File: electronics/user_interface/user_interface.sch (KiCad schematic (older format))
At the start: 48 parts, among them J1 Conn_01x06, J2 Conn_02x05_Odd_Even, U1 PCF8574, U2 PCF8574

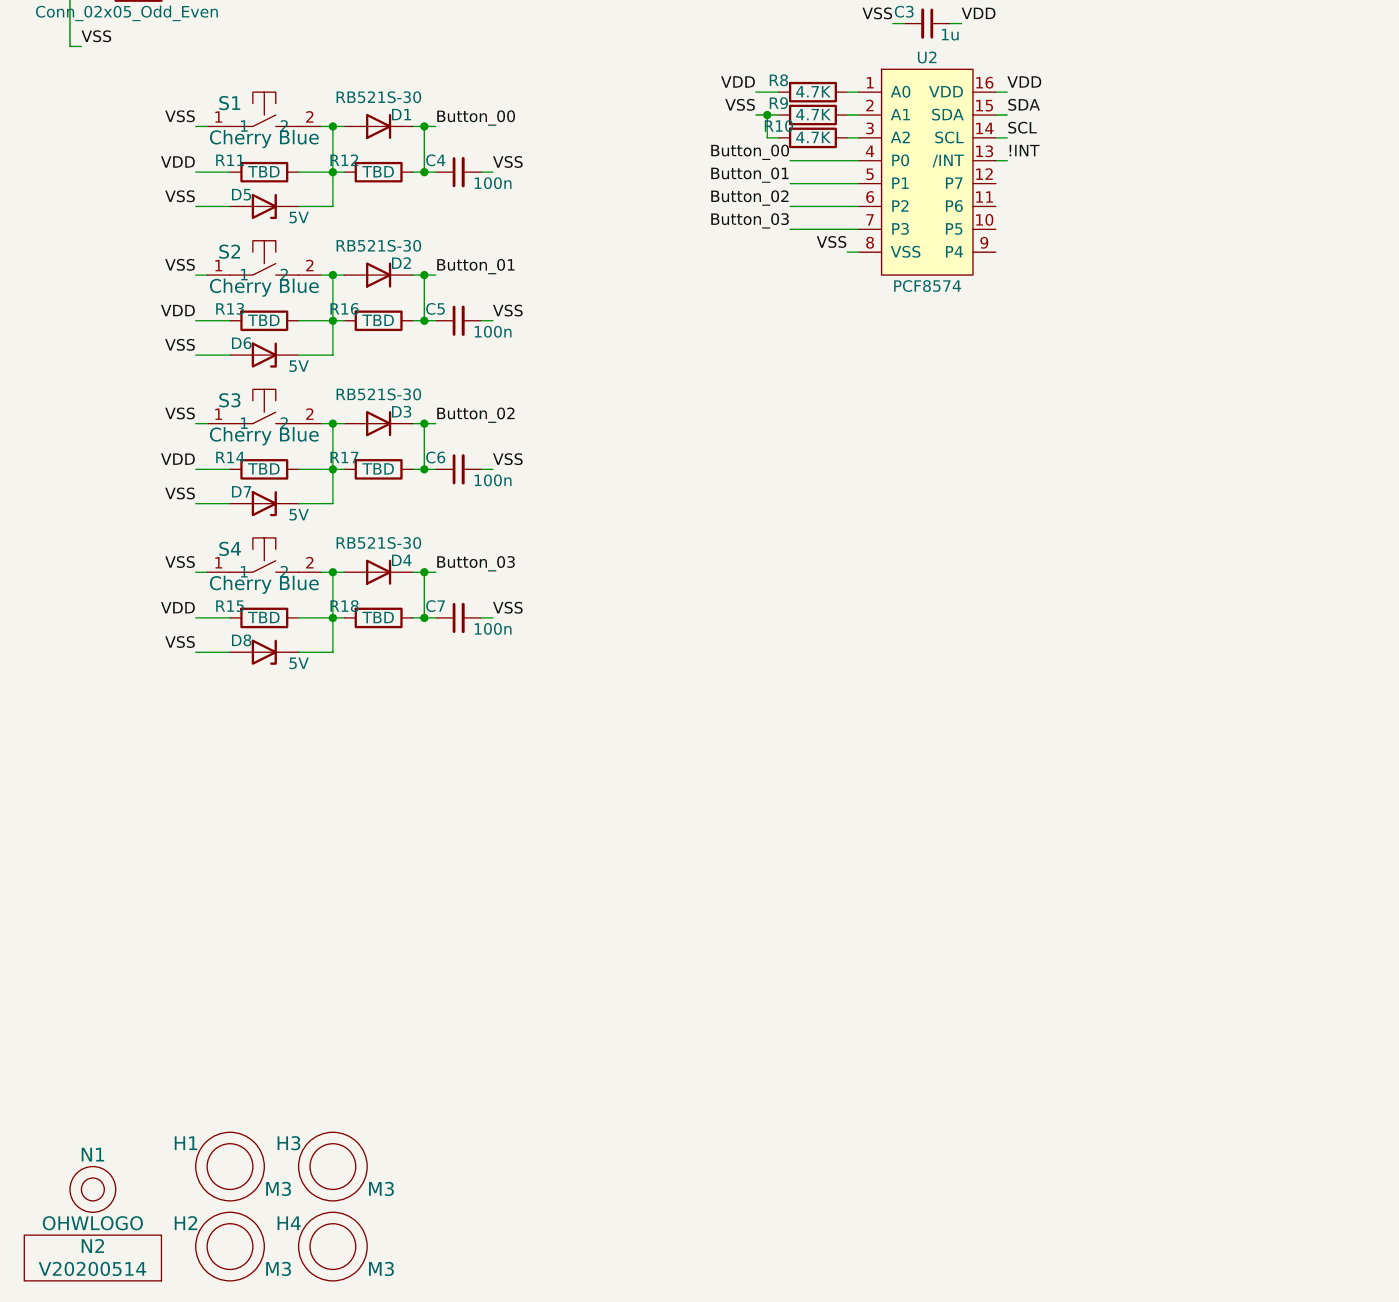
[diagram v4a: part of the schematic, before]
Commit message: rotary encoder added to schematic WIP components and debouncing
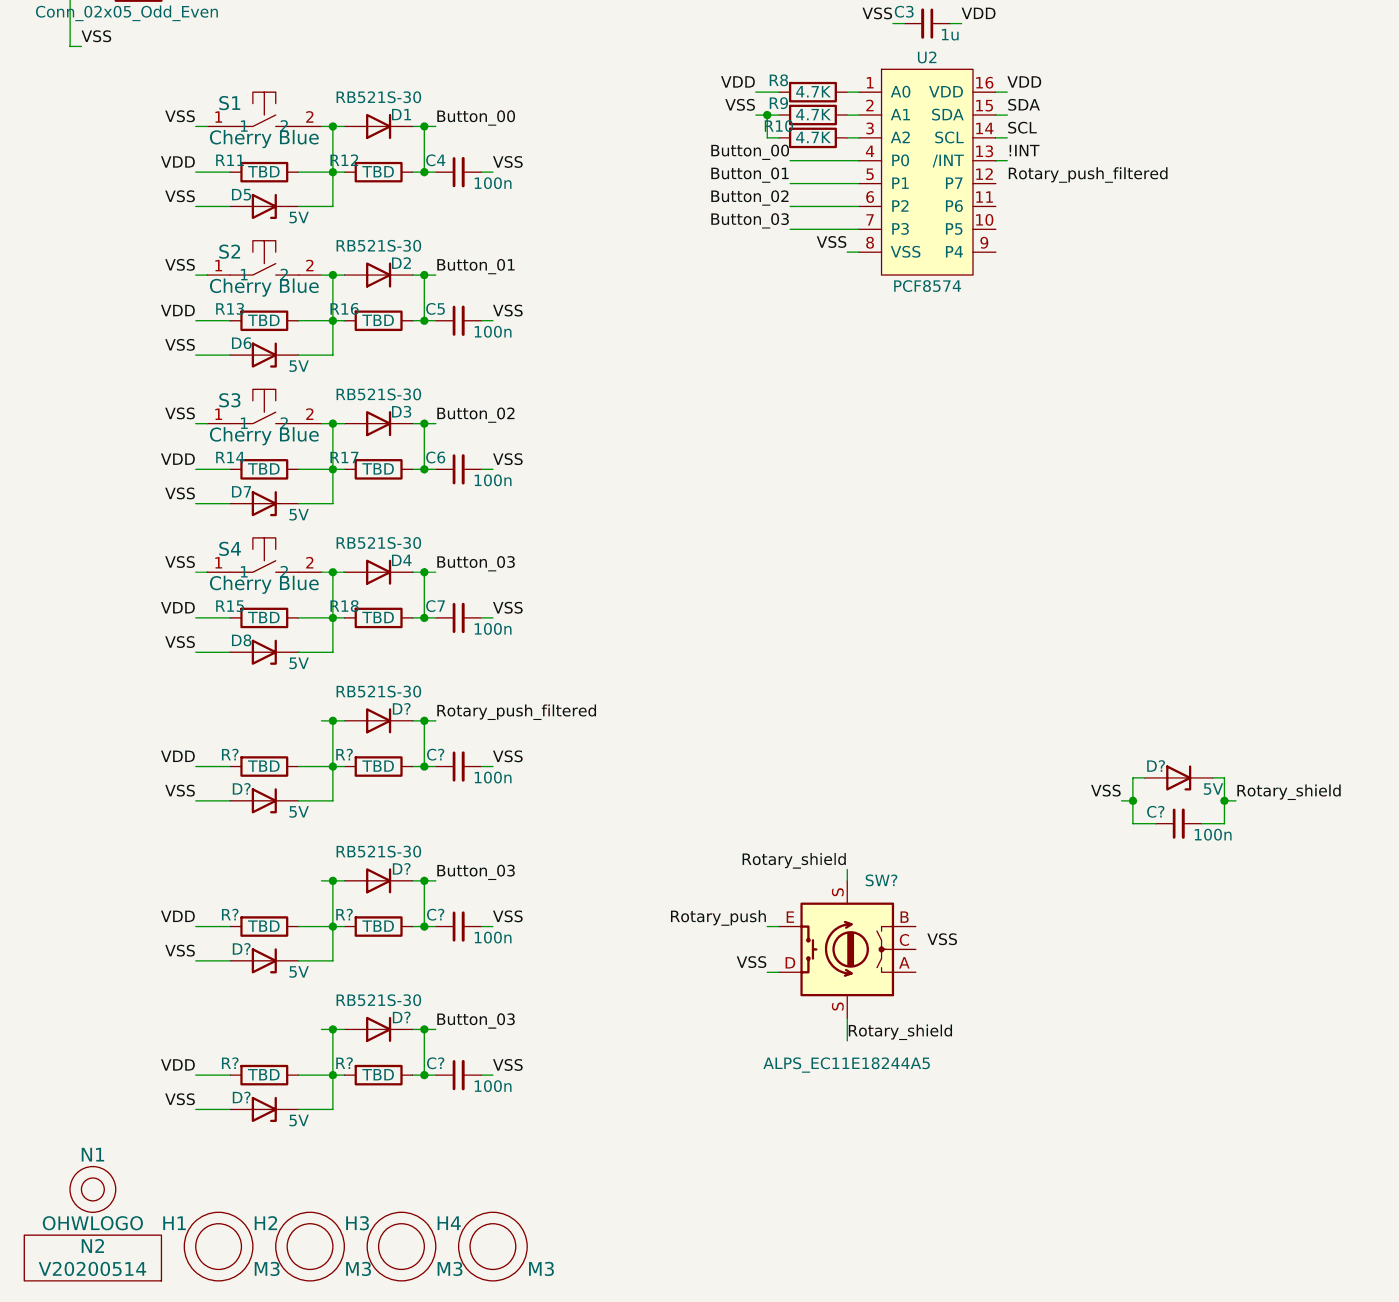
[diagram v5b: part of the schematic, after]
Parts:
- added C? (x4): 100n, SquantorRcl:C_0603, symbol Device:C_Small
- added D? (x4): 5V, SquantorDiodes:SOD-523, symbol Device:D_Zener
- added D? (x3): RB521S-30, SquantorDiodes:SOD-523, symbol Device:D
- added R? (x6): TBD, SquantorRcl:R_0603_hand, symbol Device:R
- added SW?: ALPS_EC11E18244A5, SquantorSwitches:ALPS_EC11E_style5, symbol SquantorSwitches:Rotary_Encoder_Switch
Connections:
- net Button_03: now also C?.1, C?.1, D?.1 (K), D?.1 (K), R?.1, R?.1
- net VDD: now also R?.2, R?.2, R?.2
- net VSS: now also C?.1, C?.2, C?.2, C?.2, D?.2 (A), D?.2 (A), D?.2 (A), D?.2 (A), SW?.D
- new net: D?.1 (K), D?.2 (A), R?.1, R?.2 (x3)
- new net Rotary_push: SW?.E
- new net Rotary_push_filtered: C?.1, D?.1 (K), R?.1
- new net Rotary_shield: C?.2, D?.1 (K), SW?.S (Shield)
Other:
- moved on the sheet: H1, H2, H3, H4

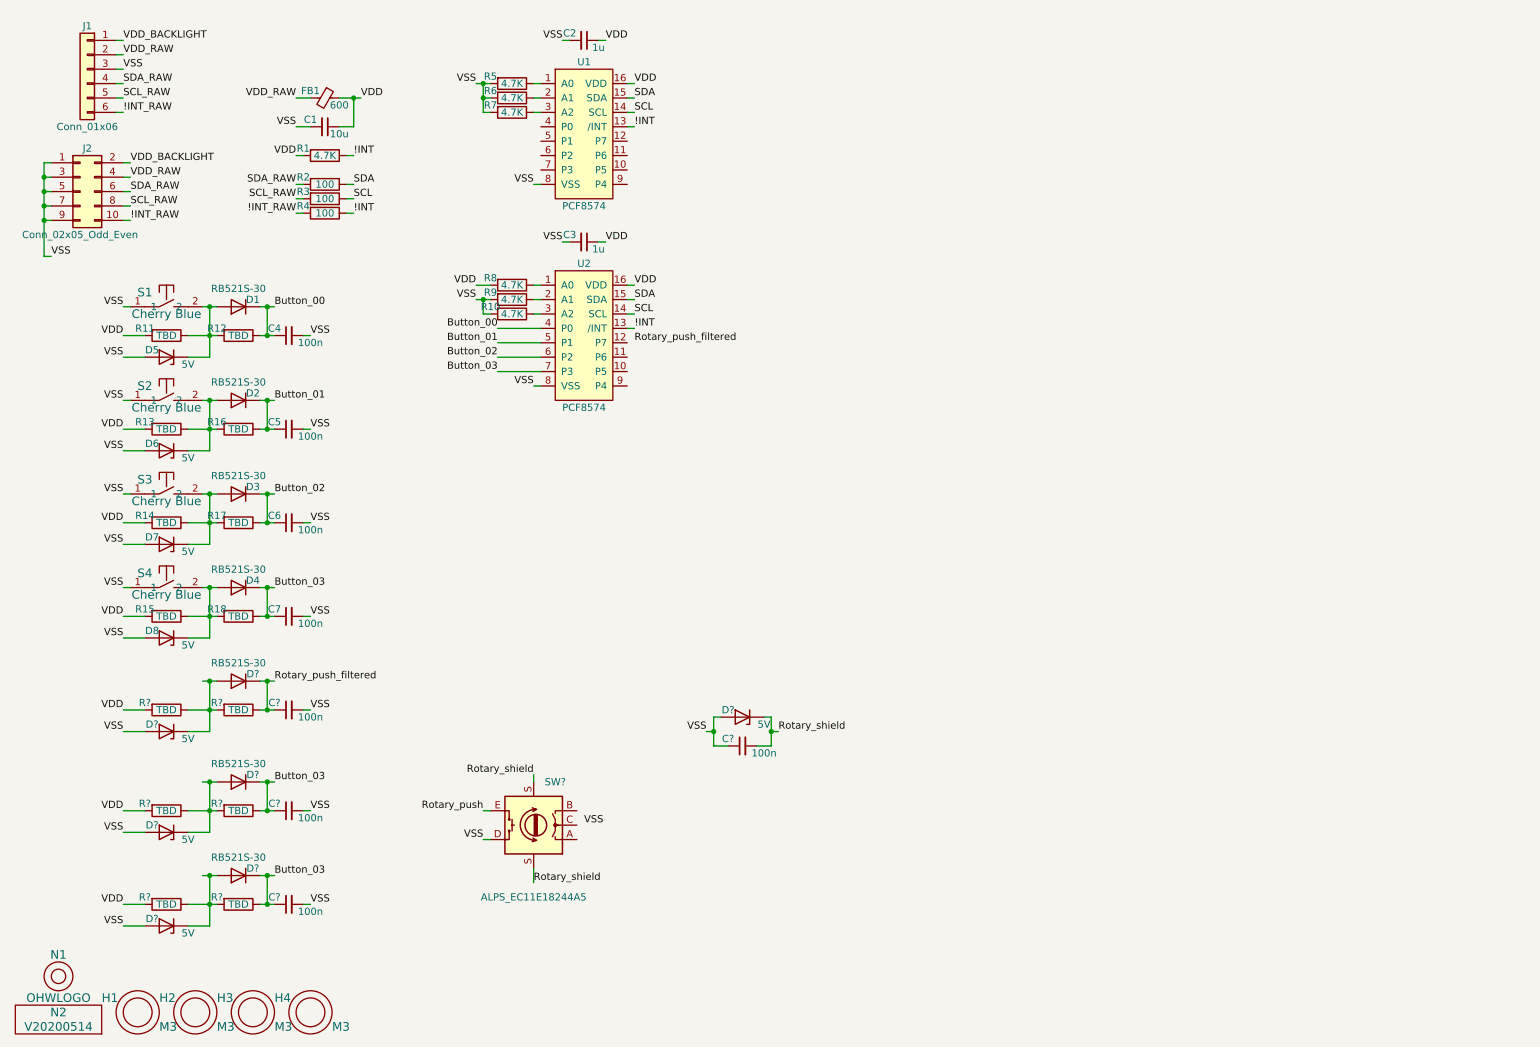
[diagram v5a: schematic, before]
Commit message: added rotary encoder knob to PCB
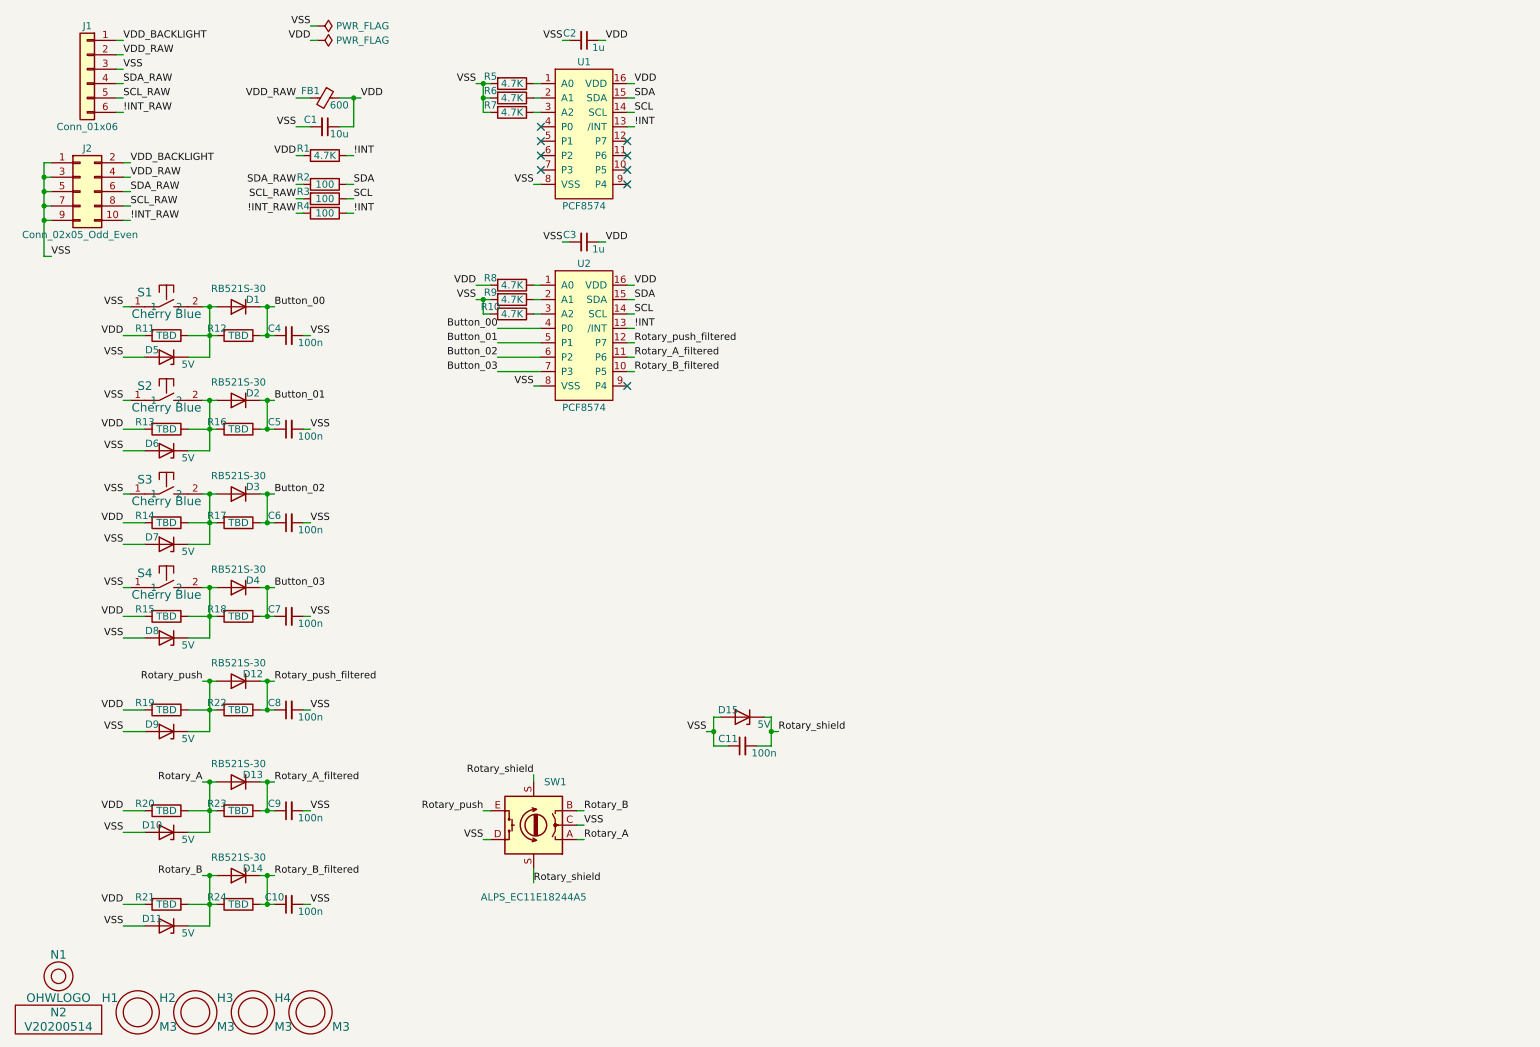
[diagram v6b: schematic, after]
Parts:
- gave numbers to parts that had none: 18
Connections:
- net Button_03: no longer C10.1, C9.1, D13.1 (K), D14.1 (K), R23.1, R24.1
- net Rotary_push: now also D12.2 (A), D9.1 (K), R19.1, R22.2
- net Rotary_push_filtered: now also U2.12 (P7)
- net VSS: now also SW1.C
- net Rotary_A: now reaches SW1.A
- net Rotary_A: now also D10.1 (K), D13.2 (A), R20.1, R23.2
- net Rotary_B: now reaches SW1.B
- net Rotary_B: now also D11.1 (K), D14.2 (A), R21.1, R24.2
- net Rotary_B_filtered: now reaches U2.10 (P5)
- net Rotary_B_filtered: now also C10.1, D14.1 (K), R24.1
- net Rotary_A_filtered: now reaches U2.11 (P6)
- net Rotary_A_filtered: now also C9.1, D13.1 (K), R23.1
- no-connect marks 0 -> 9
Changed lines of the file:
@@
 	1500 4950 1350 4950
 $Comp
-L SquantorSwitches:Rotary_Encoder_Switch SW?
+L SquantorSwitches:Rotary_Encoder_Switch SW1
 U 1 1 5EC17384
 P 4200 6250
-F 0 "SW?" V 4500 6100 50  0000 C CNN
+F 0 "SW1" V 4500 6100 50  0000 C CNN
 F 1 "ALPS_EC11E18244A5" V 3700 6250 50  0000 C CNN
 F 2 "SquantorSwitches:ALPS_EC11E_style5" V 4040 6100 50  0001 C CNN
@@
 Rotary_shield
 $Comp
-L Device:D_Zener D?
+L Device:D_Zener D15
 U 1 1 5EC29DDE
 P 5650 5500
-F 0 "D?" H 5750 5450 50  0000 C CNN
+F 0 "D15" H 5750 5450 50  0000 C CNN
 F 1 "5V" H 5500 5550 50  0000 C CNN
 F 2 "SquantorDiodes:SOD-523" H 5650 5500 50  0001 C CNN
@@
 $EndComp
 $Comp
-L Device:C_Small C?
+L Device:C_Small C11
 U 1 1 5EC2A428
 P 5650 5700
-F 0 "C?" V 5700 5800 50  0000 C CNN
+F 0 "C11" V 5700 5800 50  0000 C CNN
 F 1 "100n" V 5600 5550 50  0000 C CNN
 F 2 "SquantorRcl:C_0603" H 5650 5700 50  0001 C CNN
@@
 	5450 5600 5450 5500
 $Comp
-L Device:R R?
+L Device:R R22
 U 1 1 5EC8BB23
 P 2150 5450
-F 0 "R?" V 2100 5300 50  0000 C CNN
+F 0 "R22" V 2100 5300 50  0000 C CNN
 F 1 "TBD" V 2150 5450 50  0000 C CNN
 F 2 "SquantorRcl:R_0603_hand" V 2080 5450 50  0001 C CNN
@@
 $EndComp
 $Comp
-L Device:R R?
+L Device:R R19
 U 1 1 5EC8BB2D
 P 1650 5450
-F 0 "R?" V 1600 5300 50  0000 C CNN
+F 0 "R19" V 1600 5300 50  0000 C CNN
 F 1 "TBD" V 1650 5450 50  0000 C CNN
 F 2 "SquantorRcl:R_0603_hand" V 1580 5450 50  0001 C CNN
@@
 	2000 5450 1950 5450
 $Comp
-L Device:C_Small C?
+L Device:C_Small C8
 U 1 1 5EC8BB3A
 P 2500 5450
-F 0 "C?" V 2550 5550 50  0000 C CNN
+F 0 "C8" V 2550 5550 50  0000 C CNN
 F 1 "100n" V 2450 5300 50  0000 C CNN
 F 2 "SquantorRcl:C_0603" H 2500 5450 50  0001 C CNN
@@
 	2600 5450 2650 5450
 $Comp
-L Device:D D?
+L Device:D D12
 U 1 1 5EC8BB48
 P 2150 5250
-F 0 "D?" H 2050 5200 50  0000 C CNN
+F 0 "D12" H 2050 5200 50  0000 C CNN
 F 1 "RB521S-30" H 2150 5124 50  0000 C CNN
 F 2 "SquantorDiodes:SOD-523" H 2150 5250 50  0001 C CNN
@@
 Connection ~ 2350 5250
 $Comp
-L Device:D_Zener D?
+L Device:D_Zener D9
 U 1 1 5EC8BB5E
 P 1650 5600
-F 0 "D?" H 1750 5550 50  0000 C CNN
+F 0 "D9" H 1750 5550 50  0000 C CNN
 F 1 "5V" H 1500 5650 50  0000 C CNN
 F 2 "SquantorDiodes:SOD-523" H 1650 5600 50  0001 C CNN
@@
 	1500 5600 1350 5600
 $Comp
-L Device:R R?
+L Device:R R23
 U 1 1 5ECA5BE7
 P 2150 6150
-F 0 "R?" V 2100 6000 50  0000 C CNN
+F 0 "R23" V 2100 6000 50  0000 C CNN
 F 1 "TBD" V 2150 6150 50  0000 C CNN
 F 2 "SquantorRcl:R_0603_hand" V 2080 6150 50  0001 C CNN
@@
 $EndComp
 $Comp
-L Device:R R?
+L Device:R R20
 U 1 1 5ECA5BF1
 P 1650 6150
-F 0 "R?" V 1600 6000 50  0000 C CNN
+F 0 "R20" V 1600 6000 50  0000 C CNN
 F 1 "TBD" V 1650 6150 50  0000 C CNN
 F 2 "SquantorRcl:R_0603_hand" V 1580 6150 50  0001 C CNN
@@
 	2000 6150 1950 6150
 $Comp
-L Device:C_Small C?
+L Device:C_Small C9
 U 1 1 5ECA5BFE
 P 2500 6150
-F 0 "C?" V 2550 6250 50  0000 C CNN
+F 0 "C9" V 2550 6250 50  0000 C CNN
 F 1 "100n" V 2450 6000 50  0000 C CNN
 F 2 "SquantorRcl:C_0603" H 2500 6150 50  0001 C CNN
@@
 	2600 6150 2650 6150
 $Comp
-L Device:D D?
+L Device:D D13
 U 1 1 5ECA5C0C
 P 2150 5950
-F 0 "D?" H 2050 5900 50  0000 C CNN
+F 0 "D13" H 2050 5900 50  0000 C CNN
 F 1 "RB521S-30" H 2150 5824 50  0000 C CNN
 F 2 "SquantorDiodes:SOD-523" H 2150 5950 50  0001 C CNN
@@
 	2350 5950 2350 6150
 Connection ~ 2350 6150
-Text Label 2400 5950 0    50   ~ 0
-Button_03
 Wire Wire Line
 	1900 5950 1950 5950
@@
 Connection ~ 2350 5950
 $Comp
-L Device:D_Zener D?
+L Device:D_Zener D10
 U 1 1 5ECA5C22
 P 1650 6300
-F 0 "D?" H 1750 6250 50  0000 C CNN
+F 0 "D10" H 1750 6250 50  0000 C CNN
 F 1 "5V" H 1500 6350 50  0000 C CNN
 F 2 "SquantorDiodes:SOD-523" H 1650 6300 50  0001 C CNN
@@
 	1500 6300 1350 6300
 $Comp
-L Device:R R?
+L Device:R R24
 U 1 1 5ECA5C3C
 P 2150 6800
-F 0 "R?" V 2100 6650 50  0000 C CNN
+F 0 "R24" V 2100 6650 50  0000 C CNN
 F 1 "TBD" V 2150 6800 50  0000 C CNN
 F 2 "SquantorRcl:R_0603_hand" V 2080 6800 50  0001 C CNN
@@
 $EndComp
 $Comp
-L Device:R R?
+L Device:R R21
 U 1 1 5ECA5C46
 P 1650 6800
-F 0 "R?" V 1600 6650 50  0000 C CNN
+F 0 "R21" V 1600 6650 50  0000 C CNN
 F 1 "TBD" V 1650 6800 50  0000 C CNN
 F 2 "SquantorRcl:R_0603_hand" V 1580 6800 50  0001 C CNN
@@
 	2000 6800 1950 6800
 $Comp
-L Device:C_Small C?
+L Device:C_Small C10
 U 1 1 5ECA5C53
 P 2500 6800
-F 0 "C?" V 2550 6900 50  0000 C CNN
+F 0 "C10" V 2550 6900 50  0000 C CNN
 F 1 "100n" V 2450 6650 50  0000 C CNN
 F 2 "SquantorRcl:C_0603" H 2500 6800 50  0001 C CNN
@@
 	2600 6800 2650 6800
 $Comp
-L Device:D D?
+L Device:D D14
 U 1 1 5ECA5C61
 P 2150 6600
-F 0 "D?" H 2050 6550 50  0000 C CNN
+F 0 "D14" H 2050 6550 50  0000 C CNN
 F 1 "RB521S-30" H 2150 6474 50  0000 C CNN
 F 2 "SquantorDiodes:SOD-523" H 2150 6600 50  0001 C CNN
@@
 	2350 6600 2350 6800
 Connection ~ 2350 6800
-Text Label 2400 6600 0    50   ~ 0
-Button_03
 Wire Wire Line
 	1900 6600 1950 6600
@@
 Connection ~ 2350 6600
 $Comp
-L Device:D_Zener D?
+L Device:D_Zener D11
 U 1 1 5ECA5C77
 P 1650 6950
-F 0 "D?" H 1750 6900 50  0000 C CNN
+F 0 "D11" H 1750 6900 50  0000 C CNN
 F 1 "5V" H 1500 7000 50  0000 C CNN
 F 2 "SquantorDiodes:SOD-523" H 1650 6950 50  0001 C CNN
@@
 Wire Wire Line
 	3900 6350 3850 6350
+Wire Wire Line
+	4550 6250 4500 6250
+Text Label 4550 6350 0    50   ~ 0
+Rotary_A
+Text Label 4550 6150 0    50   ~ 0
+Rotary_B
+Wire Wire Line
+	4500 6150 4550 6150
+Wire Wire Line
+	4550 6350 4500 6350
+Text Label 1900 5250 2    50   ~ 0
+Rotary_push
+Text Label 1900 5950 2    50   ~ 0
+Rotary_A
+Text Label 1900 6600 2    50   ~ 0
+Rotary_B
+Text Label 2400 5950 0    50   ~ 0
+Rotary_A_filtered
+Text Label 2400 6600 0    50   ~ 0
+Rotary_B_filtered
+Text Label 4900 3000 0    50   ~ 0
+Rotary_A_filtered
+Text Label 4900 3100 0    50   ~ 0
+Rotary_B_filtered
+Wire Wire Line
+	4900 2900 4850 2900
+Wire Wire Line
+	4850 3000 4900 3000
+Wire Wire Line
+	4900 3100 4850 3100
+$Comp
+L power:PWR_FLAG #FLG0101
+U 1 1 5ED8E672
+P 2700 700
+F 0 "#FLG0101" H 2700 775 50  0001 C CNN
+F 1 "PWR_FLAG" V 2700 828 50  0000 L CNN
+F 2 "" H 2700 700 50  0001 C CNN
+F 3 "~" H 2700 700 50  0001 C CNN
+	1    2700 700
+	0    1    1    0
+$EndComp
+Text Label 2650 700  2    50   ~ 0
+VSS
+Text Label 2650 800  2    50   ~ 0
+VDD
+$Comp
+L power:PWR_FLAG #FLG0102
+U 1 1 5ED8FA16
+P 2700 800
+F 0 "#FLG0102" H 2700 875 50  0001 C CNN
+F 1 "PWR_FLAG" V 2700 928 50  0000 L CNN
+F 2 "" H 2700 800 50  0001 C CNN
+F 3 "~" H 2700 800 50  0001 C CNN
+	1    2700 800
+	0    1    1    0
+$EndComp
+Wire Wire Line
+	2650 700  2700 700
+Wire Wire Line
+	2700 800  2650 800
+NoConn ~ 4850 3200
+NoConn ~ 4250 1400
+NoConn ~ 4250 1500
+NoConn ~ 4250 1600
+NoConn ~ 4250 1700
+NoConn ~ 4850 1800
+NoConn ~ 4850 1700
+NoConn ~ 4850 1600
+NoConn ~ 4850 1500
 $EndSCHEMATC
